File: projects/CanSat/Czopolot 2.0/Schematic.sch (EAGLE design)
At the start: 98 parts

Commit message: Microcontroller and sensors done...
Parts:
- removed C40, C41: 100n, Unified:CAPACITOR0603
- removed C43, C44: 10u, Unified:CAPACITOR0603
- removed MOTL, MOTR: MOTOR, Unified:MOTOR
- removed R1, R13: 4.7k, Unified:RESISTOR0603
- removed R12, R14, R3: 100k, Unified:RESISTOR0603
- removed R40, R41, R7, R70, R71, R72, R8, R9: 10k, Unified:RESISTOR0603
- removed R5: 560R, Unified:RESISTOR0603
- removed RN1: 560R, SobieskiSat2:RESISTORARRAY
- added BTN_USR1: PUSH-SWITCH, SobieskiSat2:PUSH-SWITCH
- added U$12: TC78H653FTG, SobieskiSat2:TC78H653FTG
- added U$13: MOTORJST_SMD, Unified:MOTORJST_SMD
- added U$16, U$26: RESISTORARRAY, SobieskiSat2:RESISTORARRAY
- added U$17, U$18: CONNECTOR_F_X2_JST_SMD, Unified:CONNECTOR_F_X2_JST_SMD
- added U$19, U$20, U$24, U$25: CONNECTOR_F_X3_JST_SMD, Unified:CONNECTOR_F_X3_JST_SMD
- added X1: FH12-24S-0.5SH, con-hirose:FH12-24S-0.5SH
- BAT_PACK: device SobieskiSat2:BATTERYBIG -> SobieskiSat2:BATTERYJST
- BTN_DFU: value PUSH-SWITCHDIP -> SLIDE-SWITCH; device SobieskiSat2:PUSH-SWITCHDIP -> SobieskiSat2:SLIDE-SWITCH
- U$14: value DRV8838 -> MOTORJST_SMD; device SobieskiSat2:DRV8838 -> Unified:MOTORJST_SMD
- U$15: value DRV8838 -> RESISTORARRAY; device SobieskiSat2:DRV8838 -> SobieskiSat2:RESISTORARRAY
- U$4: value SLIDE-SWITCH -> RESISTORARRAY; device SobieskiSat2:SLIDE-SWITCH -> SobieskiSat2:RESISTORARRAY
- U$7: value USB-C -> USB2.0; device SobieskiSat2:USB-C -> SobieskiSat2:USB2.0
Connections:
- removed net EN_L: U$14.EN, U$1STM32F405RGT6_GPIO.PA1
- removed net EN_R: U$15.EN, U$1STM32F405RGT6_GPIO.PA3
- removed net GPIO_S1: U$11.6, U$1STM32F405RGT6_GPIO.PB0
- removed net GPIO_S2: U$11.10, U$1STM32F405RGT6_GPIO.PB1
- removed net N$23: C70.2, U$9.REGOUT
- removed net N$31: R40.1, U$14.NSLP
- removed net N$34: MOTR.P$2, U$15.OUT1
- removed net N$36: MOTR.P$1, U$15.OUT2
- removed net N$40: R41.1, U$15.NSLP
- removed net PH_L: U$14.PH, U$1STM32F405RGT6_GPIO.PA0
- removed net PH_R: U$15.PH, U$1STM32F405RGT6_GPIO.PA2
- new net EN_1: U$1STM32F405RGT6_GPIO.PB12
- new net EN_2: U$1STM32F405RGT6_GPIO.PB13
- new net EN_3: U$1STM32F405RGT6_GPIO.PB14
- new net EN_4: U$1STM32F405RGT6_GPIO.PB15
- new net MPU_REG: C70.2, U$9G$1.REGOUT, U$9G$2.P14
- new net N$25: R0.1
- new net N$7: BTN_USR.P$1, U$16G$4.1
- new net PWM_1: U$1STM32F405RGT6_GPIO.PB1
- new net PWM_2: U$1STM32F405RGT6_GPIO.PB0
- new net PWM_3: U$1STM32F405RGT6_GPIO.PC6
- new net PWM_4: U$1STM32F405RGT6_GPIO.PC7
- net 43_D0: now also U$1STM32F405RGT6_GPIO.PC4; no longer U$1STM32F405RGT6_GPIO.PC5
- net 43_D1: now also U$1STM32F405RGT6_GPIO.PC5; no longer U$1STM32F405RGT6_GPIO.PC4
- net 43_MOSI: now also U$26G$1.2; no longer R3.2
- net 43_NSS: now also U$1STM32F405RGT6_GPIO.PC13; no longer U$1STM32F405RGT6_GPIO.PB8
- net 43_RST: now also U$1STM32F405RGT6_GPIO.PA15; no longer R2.2, U$1STM32F405RGT6_GPIO.PB2
- net BAT: no longer C40.2, C43.2, U$14.VM, U$15.VM
- net BMP_SDI: now also U$26G$2.2; no longer R9.1
- net BMP_SDO: now also U$26G$3.2; no longer R8.2
- net DFU: now also U$16G$2.2; no longer BTN_DFU.P$2, R12.1
- net GND: now also U$9G$1.FSYNC, U$9G$1.GND, U$9G$1.RESV2, U$9G$2.P5; no longer BTN_USR.P$1, C40.1, C41.1, C43.1, C44.1, R0.1, R12.2, R8.1, U$14.GND, U$15.GND, U$9.FSYNC, U$9.GND, U$9.RESV2
- net GPIO_RX: no longer U$1STM32F405RGT6_GPIO.PC7
- net GPIO_TX: no longer U$1STM32F405RGT6_GPIO.PC6
- net IMU_INT: now also U$9G$1.INT; no longer U$1STM32F405RGT6_GPIO.PB9, U$9.INT
- net MPU_AD0: now also U$15G$1.2, U$9G$1.AD0/SDO, U$9G$2.P15; no longer R72.1, U$9.AD0/SDO
- net MPU_ECL: now also U$9G$1.AUX_CL; no longer U$9.AUX_CL
- net MPU_EDA: now also U$9G$1.AUX_DA; no longer U$9.AUX_DA
- net MPU_NCS: now also U$15G$2.2, U$9G$1.NCS; no longer R7.1, U$9.NCS
- net N$1: now also U$4G$1.1; no longer RN1G$2.2
- net N$10: no longer RN1G$1.1
- net N$15: now also U$1STM32F405RGT6_GPIO.PC0, U$4G$4.2; no longer R5.2, U$1STM32F405RGT6_GPIO.PB15
- net N$16: now also BTN_USR1.P$1, U$16G$3.2; no longer BTN_USR.P$2, R1.1
- net N$19: now also U$1STM32F405RGT6_GPIO.PC3, U$4G$1.2; no longer RN1G$4.1, U$1STM32F405RGT6_GPIO.PB14
- net N$2: now also U$4G$2.1; no longer RN1G$3.2
- net N$20: now also U$1STM32F405RGT6_GPIO.PC2, U$4G$2.2; no longer RN1G$3.1, U$1STM32F405RGT6_GPIO.PB13
- net N$26: now also U$1STM32F405RGT6_GPIO.PC1, U$4G$3.2; no longer MOTL.P$1, U$14.OUT2
- net N$28: now also BTN_USR1.P$2, U$1STM32F405RGT6_GPIO.PB8; no longer RN1G$2.1, U$1STM32F405RGT6_GPIO.PB12
- net N$3: no longer RN1G$1.2
- net N$37: now also U$4G$3.1; no longer RN1G$4.2
- net N$38: now also U$4G$4.1; no longer R5.1
- net N$4: now also R2.2, U$1STM32F405RGT6_GPIO.PB2; no longer R1.2, U$1STM32F405RGT6_GPIO.PA15
- net N$5: now also BTN_USR.P$2, U$1STM32F405RGT6_GPIO.PB9; no longer MOTL.P$2, U$14.OUT1
- net NRST: now also U$26G$4.2; no longer R13.1
- net SCL: now also U$15G$3.2, U$9G$1.SCL/SCK, U$9G$2.P3; no longer R71.1, U$9.SCL/SCK
- net SDA: now also U$15G$4.2, U$9G$1.SDA/SDI, U$9G$2.P2; no longer R70.1, U$9.SDA/SDI
- net SD_D3: now also U$16G$1.2; no longer R14.2
- net VCC: now also U$15G$1.1, U$15G$2.1, U$15G$3.1, U$15G$4.1, U$16G$1.1, U$16G$2.1, U$16G$3.1, U$16G$4.2, U$26G$1.1, U$26G$2.1, U$26G$3.1, U$26G$4.1, U$9G$1.RESV1, U$9G$1.VDD, U$9G$1.VDDIO; no longer BTN_DFU.P$1, C41.2, C44.2, LEDP.P$1, R13.2, R14.1, R3.1, R40.2, R41.2, R7.2, R70.2, R71.2, R72.2, R9.2, U$14.VCC, U$15.VCC, U$9.RESV1, U$9.VDD, U$9.VDDIO
- net VSYS: now also LEDP.P$1
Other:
- note added: "Motor drivers - TC78H653FTG"
- note removed: "Motor drivers - DRV8838"
- moved on the sheet: BTN_USR, LEDA, LEDB, LEDC, LEDD, LEDP, R30

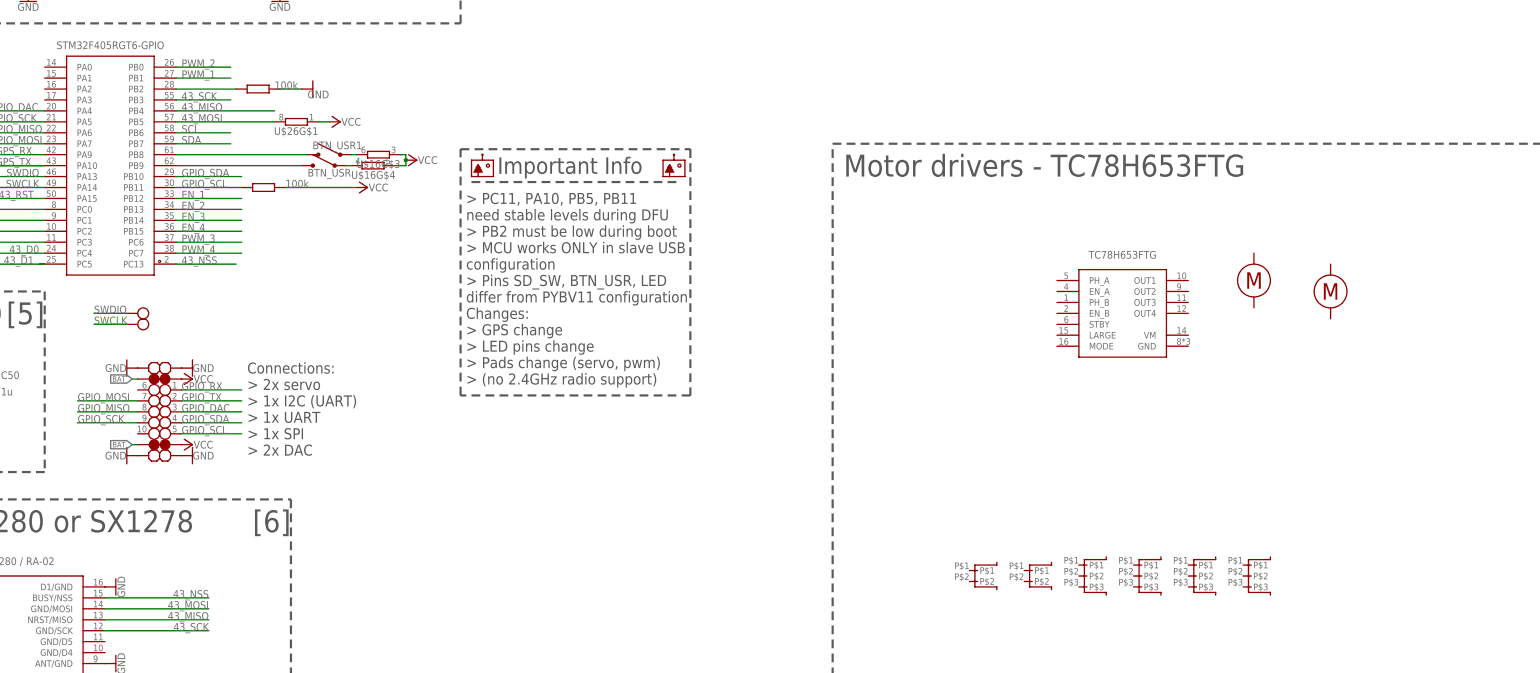
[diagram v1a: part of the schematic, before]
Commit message: Dual motor connectors added
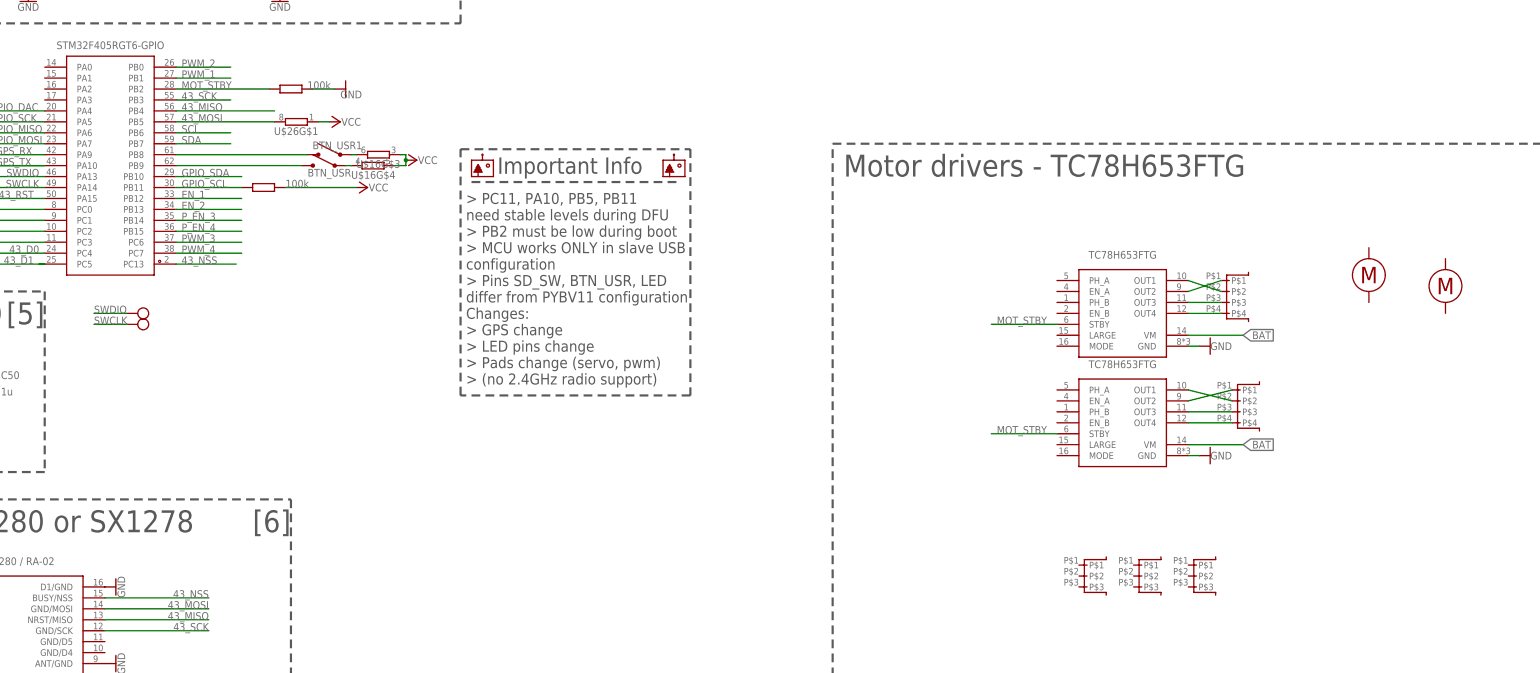
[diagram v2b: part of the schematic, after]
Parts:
- removed U$25: CONNECTOR_F_X3_JST_SMD, Unified:CONNECTOR_F_X3_JST_SMD
- U$11: value GPIO_PADS2 -> TC78H653FTG; device SobieskiSat2:GPIO_PADS2 -> SobieskiSat2:TC78H653FTG
- U$17, U$18: value CONNECTOR_F_X2_JST_SMD -> CONNECTOR_F_X4_JST_SMD; device Unified:CONNECTOR_F_X2_JST_SMD -> Unified:CONNECTOR_F_X4_JST_SMD
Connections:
- net EN_3 renamed P_EN_3
- net EN_4 renamed P_EN_4
- removed net GPIO_RX: U$11.1
- removed net GPIO_TX: U$11.2
- new net MOT_STBY: R2.2, U$11.STBY, U$12.STBY, U$1STM32F405RGT6_GPIO.PB2
- new net N$23: U$11.OUT1, U$18.P$2
- new net N$29: U$11.OUT3, U$18.P$3
- new net N$30: U$11.OUT4, U$18.P$4
- new net N$31: U$12.OUT2, U$17.P$1
- new net N$33: U$12.OUT1, U$17.P$2
- new net N$34: U$12.OUT3, U$17.P$3
- new net N$35: U$12.OUT4, U$17.P$4
- net BAT: now also U$11.VM, U$12.VM; no longer U$11.VBAT$1, U$11.VBAT$2
- net GND: now also U$11.GND, U$12.GND; no longer U$11.GND$1, U$11.GND$2, U$11.GND$3, U$11.GND$4
- net GPIO_DAC: no longer U$11.3
- net GPIO_MISO: no longer U$11.8
- net GPIO_MOSI: no longer U$11.7
- net GPIO_SCK: no longer U$11.9
- net GPIO_SCL: no longer U$11.5
- net GPIO_SDA: no longer U$11.4
- net N$4: now also U$11.OUT2, U$18.P$1; no longer R2.2, U$1STM32F405RGT6_GPIO.PB2
- net VCC: no longer U$11.VCC$1, U$11.VCC$2
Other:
- note removed: "Connections: > 2x servo > 1x I2C (UART) > 1x UART > 1x SPI > 2x DAC"

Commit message: V2 work...
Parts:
- removed THR: NTC, SobieskiSat2:NTC
- added C17, C18: 100n, Unified:CAPACITOR0603
- added GND, VCC: PADTEST, Unified:PADTEST
- added R1, R5: 10k, Unified:RESISTOR0603
- added R3, R7: 10k, SobieskiSat2:DOUBLE_RESISTOR
- added R8: 1k, Unified:RESISTOR0603
- added U$25: GPIO_PADS, SobieskiSat2:GPIO_PADS
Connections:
- removed net GPS_RST: U$3.RST
- removed net N$22: R22.1, R23.2, R24.1, THR.1
- removed net N$25: R0.1
- new net N$36: R1.2, U$12.MODE
- new net N$39: R3.P$1, U$12.LARGE
- new net N$40: R5.2, U$11.MODE
- new net N$42: R7.P$1, U$11.LARGE
- new net NTC: R22.1, R23.2, R24.1, U$24.P$3
- new net UART2_RX: U$1STM32F405RGT6_GPIO.PA3, X1-6.1
- new net UART2_TX: U$1STM32F405RGT6_GPIO.PA2, X1-5.1
- new net UART4_RX: U$1STM32F405RGT6_GPIO.PA1, X1-4.1
- new net UART4_TX: U$1STM32F405RGT6_GPIO.PA0, X1-3.1
- net BAT: now also C17.1, C18.1, U$19.P$2, U$20.P$2, U$24.P$2, X1-21.1, X1-22.1
- net DFU: now also U$3.RST
- net EN_1: now also U$12.PH_A, X1-13.1
- net EN_2: now also U$12.PH_B, X1-14.1
- net GND: now also C17.2, C18.2, GND.1, R0.1, R3.P$3, R7.P$3, U$19.P$1, U$20.P$1, U$24.P$1, X1-1.1, X1-17.1, X1-23.1, X1-7.1; no longer THR.2
- net GPIO_DAC: now also X1-9.1
- net GPIO_MISO: now also X1-11.1
- net GPIO_MOSI: now also X1-12.1
- net GPIO_SCK: now also X1-10.1
- net GPIO_SCL: now also X1-20.1
- net GPIO_SDA: now also X1-19.1
- net N$10: now also R8.1
- net N$3: now also R8.2
- net PWM_1: now also U$12.EN_B, X1-16.1
- net PWM_2: now also U$12.EN_A, X1-15.1
- net PWM_3: now also U$11.EN_B
- net PWM_4: now also U$11.EN_A
- net P_EN_3: now also U$11.PH_A
- net P_EN_4: now also U$11.PH_B
- net VCC: now also R1.1, R3.P$2, R5.1, R7.P$2, VCC.1, X1-18.1, X1-2.1, X1-24.1, X1-8.1

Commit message: V2 almost done
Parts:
- removed BAT_PACK: (no value), SobieskiSat2:BATTERYJST
- removed CLK, D+, D-, DIO, GND, VCC: PADTEST, Unified:PADTEST
- removed U$18: CONNECTOR_F_X4_JST_SMD, Unified:CONNECTOR_F_X4_JST_SMD
- removed U$24: CONNECTOR_F_X3_JST_SMD, Unified:CONNECTOR_F_X3_JST_SMD
- added C19, C25: 10u, Unified:CAPACITOR1206
- added C26, C27: 50p, Unified:CAPACITOR0603
- added C28: (no value), rcl:CPOL-US153CLV-0405
- added R10, R9: 0R, Unified:RESISTOR0603
- C2, C23: device Unified:CAPACITOR1206 -> Unified:CAPACITOR0603
- U$13: value MOTORJST_SMD -> MOTOR_DUO; device Unified:MOTORJST_SMD -> SobieskiSat2:MOTOR_DUO
- U$14: value MOTORJST_SMD -> BAT_JST_4(3); device Unified:MOTORJST_SMD -> SobieskiSat2:BAT_JST_4(3)
- U$17: value CONNECTOR_F_X4_JST_SMD -> MOTOR_DUO; device Unified:CONNECTOR_F_X4_JST_SMD -> SobieskiSat2:MOTOR_DUO
- U$25: value GPIO_PADS -> GPIO_DEBUG; device SobieskiSat2:GPIO_PADS -> SobieskiSat2:GPIO_DEBUG
- X1: device con-hirose:FH12-24S-0.5SH -> SobieskiSat2:FH12-24S-0.5SH
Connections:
- new net BAT_BQ: C23.1, R9.2, U$10.BAT
- new net GPS_RST: R10.2, U$3.RST
- new net N$25: BTN_DFU.P$1, R10.1
- net BAT: now also C19.1, C25.1, C26.1, C27.1, R1.1, R3.P$2, R5.1, R7.P$2, R9.1, U$14.+; no longer BAT_PACK.+, C23.1, U$10.BAT, U$24.P$2, X1-21.1, X1-22.1
- net DFU: now also BTN_DFU.P$3, X1-14.1; no longer U$3.RST
- net EN_1: now also X1-15.1; no longer X1-13.1
- net EN_2: now also X1-16.1; no longer X1-14.1
- net GND: now also BTN_DFU.P$2, C19.2, C25.2, C26.2, C27.2, U$13.S$1, U$14.-, U$17.S$1, U$19.S$1, U$20.S$1, U$25.P$1, U$25.P$9, X1G$1.S$1, X1G$2.S$1; no longer BAT_PACK.-, GND.1, U$24.P$1
- net GPIO_SCL: now also X1-22.1; no longer X1-20.1
- net GPIO_SDA: now also X1-21.1; no longer X1-19.1
- net N$23: now also U$13.P$2; no longer U$18.P$2
- net N$29: now also U$13.P$3; no longer U$18.P$3
- net N$30: now also U$13.P$4; no longer U$18.P$4
- net N$4: now also U$13.P$1; no longer U$18.P$1
- net NRST: now also X1-13.1
- net NTC: now also U$14.NTC; no longer U$24.P$3
- net PWM_1: now also X1-20.1; no longer X1-16.1
- net PWM_2: now also X1-19.1; no longer X1-15.1
- net PWM_3: now also U$25.P$7
- net PWM_4: now also U$11.PH_B, U$25.P$8; no longer U$11.EN_A
- net P_EN_4: now also U$11.EN_A; no longer U$11.PH_B
- net SWCLK: now also U$25.P$3; no longer CLK.1
- net SWDIO: now also U$25.P$2; no longer DIO.1
- net UART2_RX: now also U$20.P$3
- net UART2_TX: now also U$19.P$3
- net USB_D+: now also U$25.P$4; no longer D+.1
- net USB_D-: now also U$25.P$5; no longer D-.1
- net VCC: now also LEDP.P$1, U$25.P$6; no longer LEDCH.P$1, R1.1, R3.P$2, R5.1, R7.P$2, VCC.1
- net VSYS: now also LEDCH.P$1, U$14.AUX+; no longer LEDP.P$1
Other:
- moved on the sheet: C10, C17, C18, LEDCH, LEDP, R30, R8
